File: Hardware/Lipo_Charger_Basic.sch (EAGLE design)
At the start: 14 parts, among them U1 MCP73831, X1 Micro USB

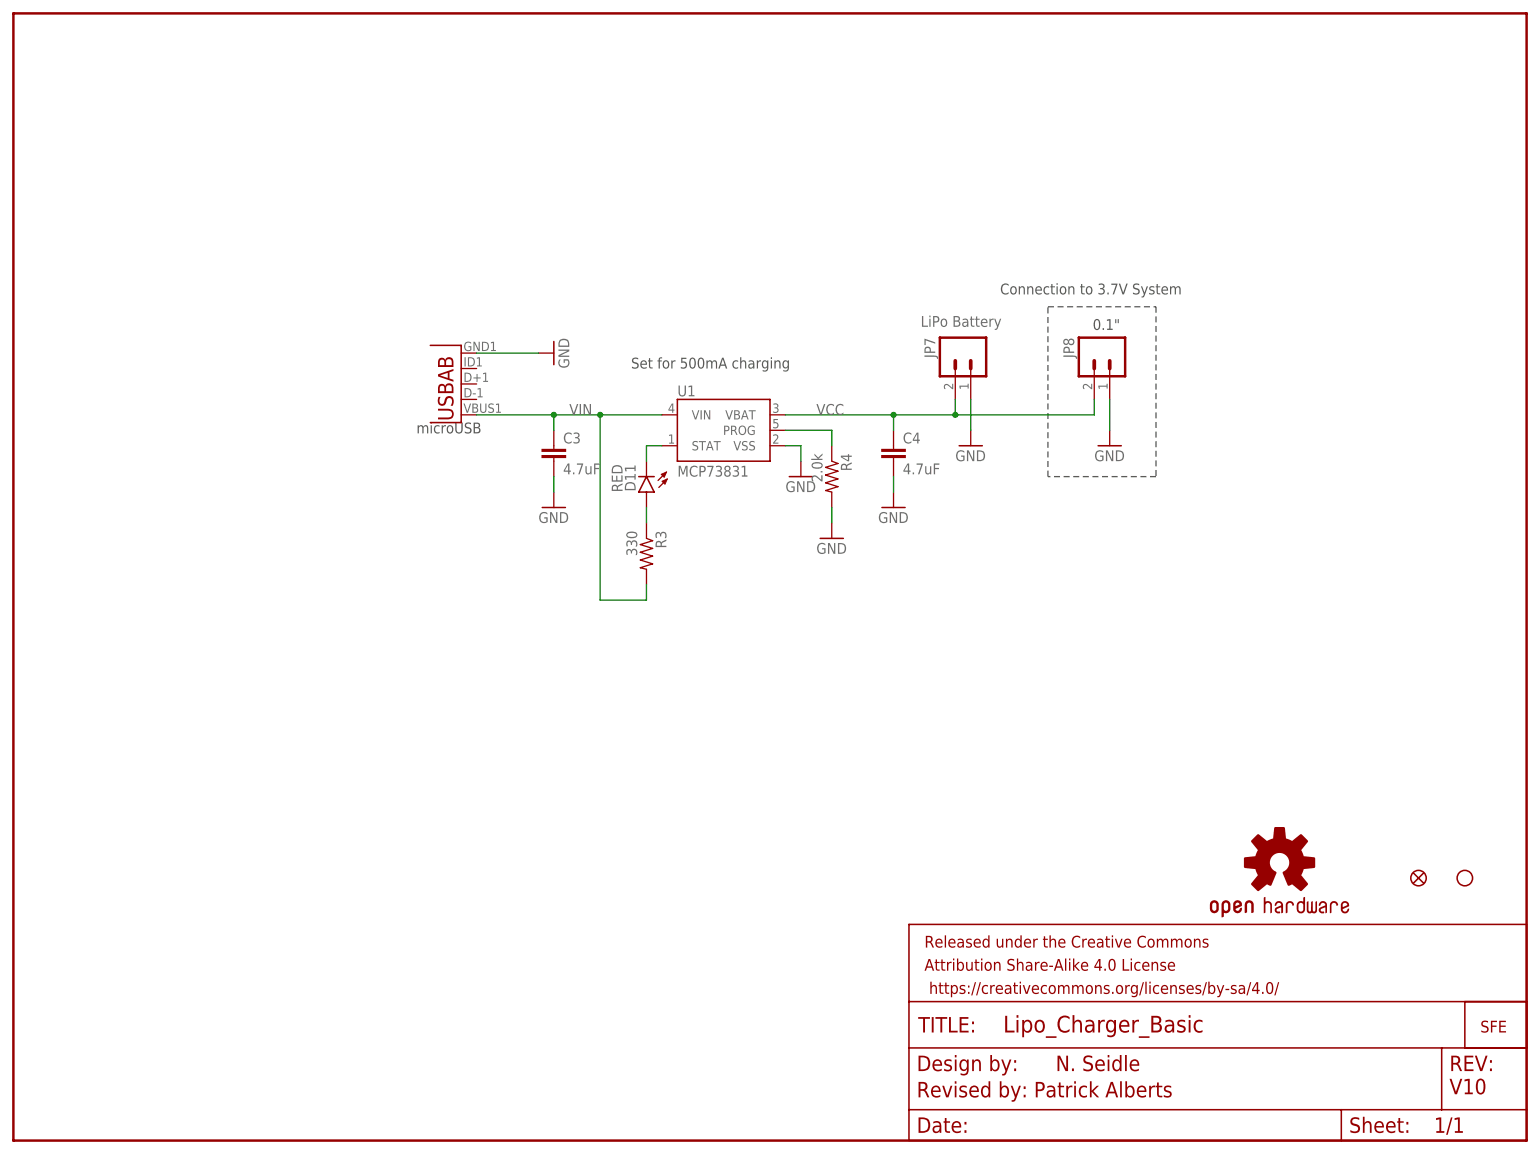
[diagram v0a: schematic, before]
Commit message: Fixed sch and moved micro B
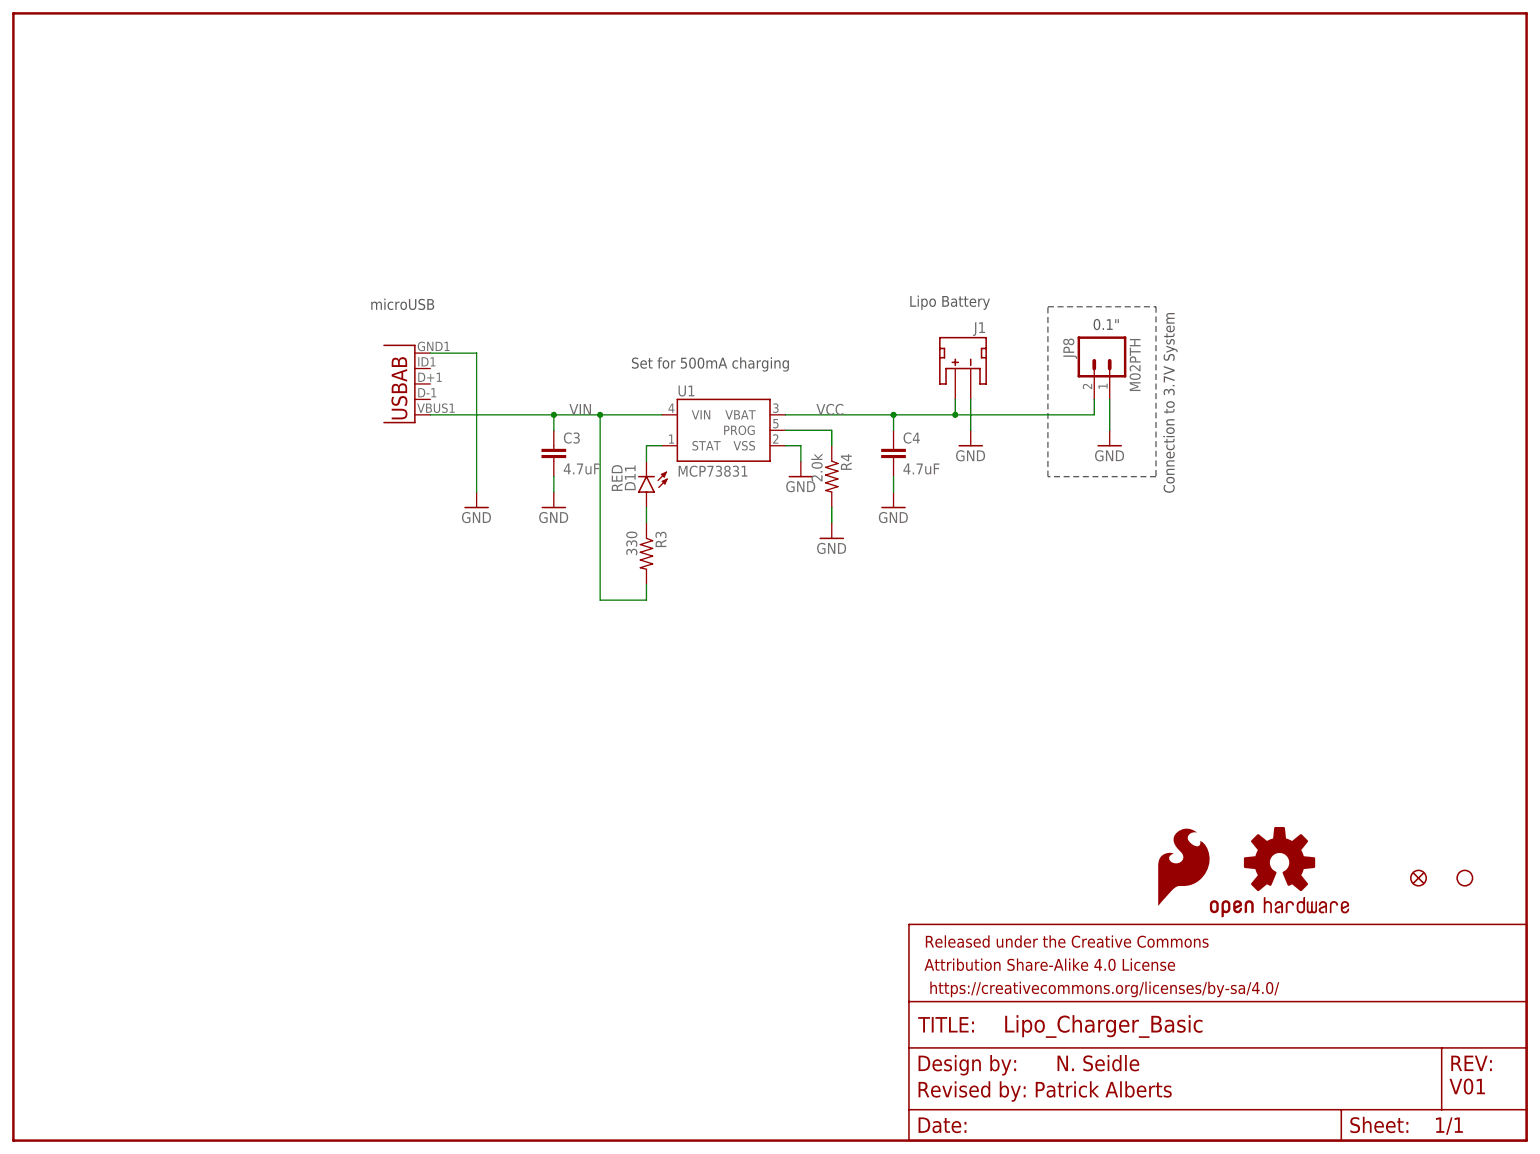
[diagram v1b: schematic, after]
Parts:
- removed JP1: LOGO-SFESK, SparkFun:LOGO-SFESK
- removed JP7: LiPo Battery, SparkFun:M02-JST-2MM-SMT
- removed X1: Micro USB, SparkFun-Connectors:USB-ABCONN-11794
- added GND: Micro USB, SparkFun-Connectors:USB-ABCONN-11794
- added J1: (no value), SparkFun-Connectors:JST_2MM_MALE
- added LOGO2: SFE_LOGO_FLAME.1_INCH, SparkFun-Aesthetics:SFE_LOGO_FLAME.1_INCH
- JP8: value (none) -> M02PTH; device SparkFun:M02PTH -> SparkFun-Connectors:M02PTH
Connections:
- net GND: now also GND.GND, J1.-; no longer JP7.1, X1.GND
- net VCC: now also J1.+; no longer JP7.2
- net VIN: now also GND.VBUS; no longer X1.VBUS
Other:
- note added: "Lipo Battery"
- note added: "V01"
- note removed: "V10"
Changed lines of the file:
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@@
 <?xml version="1.0" encoding="utf-8"?>
 <!DOCTYPE eagle SYSTEM "eagle.dtd">
-<eagle version="7.1.0">
+<eagle version="6.4">
 <drawing>
 <settings>
@@
 <layer number="56" name="wert" color="7" fill="1" visible="no" active="no"/>
 <layer number="57" name="tCAD" color="7" fill="1" visible="no" active="no"/>
+<layer number="90" name="Modules" color="5" fill="1" visible="yes" active="yes"/>
 <layer number="91" name="Nets" color="2" fill="1" visible="yes" active="yes"/>
 <layer number="92" name="Busses" color="1" fill="1" visible="yes" active="yes"/>
@@
 <part name="R4" library="SparkFun-Resistors" deviceset="2.0KOHM1/10W5%(0603)" device="" value="2.0k"/>
 <part name="GND19" library="SparkFun" deviceset="GND" device=""/>
-<part name="JP1" library="SparkFun" deviceset="LOGO-SFE" device="SK"/>
 <part name="JP2" library="SparkFun" deviceset="STAND-OFF" device=""/>
 <part name="C3" library="SparkFun-Capacitors" deviceset="4.7UF-6.3V-10%(0603)" device="0603" value="4.7uF"/>
 <part name="C4" library="SparkFun-Capacitors" deviceset="4.7UF-6.3V-10%(0603)" device="0603" value="4.7uF"/>
-<part name="JP7" library="SparkFun" deviceset="M02" device="-JST-2MM-SMT" value="LiPo Battery"/>
-<part name="JP8" library="SparkFun" deviceset="M02" device="PTH"/>
+<part name="JP8" library="SparkFun-Connectors" deviceset="M02" device="PTH"/>
 <part name="GND2" library="SparkFun" deviceset="GND" device=""/>
-<part name="X1" library="SparkFun-Connectors" deviceset="USB-AB" device="CONN-11794" value="Micro USB"/>
+<part name="GND" library="SparkFun-Connectors" deviceset="USB-AB" device="CONN-11794" value="Micro USB"/>
 <part name="JP3" library="SparkFun" deviceset="FIDUCIAL" device="1X2"/>
 <part name="LOGO1" library="SparkFun-Aesthetics" deviceset="OSHW-LOGO" device="S"/>
+<part name="LOGO2" library="SparkFun-Aesthetics" deviceset="SFE_LOGO_FLAME" device=".1_INCH"/>
+<part name="J1" library="SparkFun-Connectors" deviceset="JST_2MM_MALE" device=""/>
 </parts>
 <sheets>
@@
 <wire x1="170.18" y1="109.22" x2="170.18" y2="137.16" width="0.2032" layer="97" style="longdash"/>
 <text x="101.6" y="127" size="1.778" layer="97">Set for 500mA charging</text>
-<text x="162.306" y="139.192" size="1.778" layer="97">Connection to 3.7V System</text>
+<text x="191.008" y="106.426" size="1.778" layer="97" rot="R90">Connection to 3.7V System</text>
 <text x="177.546" y="133.35" size="1.778" layer="97">0.1"</text>
 <text x="171.45" y="11.43" size="2.54" layer="94">N. Seidle</text>
-<text x="66.294" y="116.332" size="1.778" layer="97">microUSB</text>
+<text x="58.674" y="136.652" size="1.778" layer="97">microUSB</text>
 <text x="148.59" y="7.112" size="2.54" layer="94">Revised by: Patrick Alberts</text>
-<text x="236.22" y="7.62" size="2.54" layer="94">V10</text>
+<text x="236.22" y="7.62" size="2.54" layer="94">V01</text>
+<text x="147.32" y="137.16" size="1.778" layer="97">Lipo Battery</text>
 </plain>
 <instances>
@@
 <instance part="D11" gate="G$1" x="104.14" y="106.68" rot="R180"/>
 <instance part="R3" gate="G$1" x="104.14" y="96.52" rot="R270"/>
-<instance part="GND15" gate="1" x="88.9" y="129.54" rot="R90"/>
+<instance part="GND15" gate="1" x="76.2" y="104.14"/>
 <instance part="GND14" gate="1" x="144.78" y="104.14"/>
 <instance part="GND17" gate="1" x="88.9" y="104.14"/>
@@
 <instance part="R4" gate="G$1" x="134.62" y="109.22" rot="R270"/>
 <instance part="GND19" gate="1" x="134.62" y="99.06"/>
-<instance part="JP1" gate="G$1" x="241.3" y="17.78"/>
 <instance part="JP2" gate="G$1" x="238.76" y="43.18"/>
 <instance part="C3" gate="G$1" x="88.9" y="111.76"/>
 <instance part="C4" gate="G$1" x="144.78" y="111.76"/>
-<instance part="JP7" gate="G$1" x="157.48" y="129.54" smashed="yes" rot="MR270">
-<attribute name="NAME" x="151.638" y="132.08" size="1.778" layer="95" rot="MR270"/>
-<attribute name="VALUE" x="162.56" y="133.858" size="1.778" layer="96" rot="MR0"/>
-</instance>
 <instance part="JP8" gate="G$1" x="180.34" y="129.54" rot="MR270"/>
 <instance part="GND2" gate="1" x="180.34" y="114.3"/>
-<instance part="X1" gate="G$1" x="71.12" y="124.46" rot="MR0"/>
+<instance part="GND" gate="G$1" x="63.5" y="124.46" rot="MR0"/>
 <instance part="JP3" gate="G$1" x="231.14" y="43.18"/>
 <instance part="LOGO1" gate="G$1" x="208.28" y="45.72"/>
+<instance part="LOGO2" gate="G$1" x="187.96" y="38.1"/>
+<instance part="J1" gate="G$1" x="157.48" y="127" rot="MR0"/>
 </instances>
 <busses>
@@
 </segment>
 <segment>
-<wire x1="76.2" y1="129.54" x2="86.36" y2="129.54" width="0.1524" layer="91"/>
+<wire x1="68.58" y1="129.54" x2="76.2" y2="129.54" width="0.1524" layer="91"/>
+<wire x1="76.2" y1="129.54" x2="76.2" y2="106.68" width="0.1524" layer="91"/>
 <pinref part="GND15" gate="1" pin="GND"/>
-<pinref part="X1" gate="G$1" pin="GND"/>
+<pinref part="GND" gate="G$1" pin="GND"/>
 </segment>
 <segment>
@@
 <segment>
 <wire x1="157.48" y1="121.92" x2="157.48" y2="116.84" width="0.1524" layer="91"/>
-<pinref part="JP7" gate="G$1" pin="1"/>
 <pinref part="GND1" gate="1" pin="GND"/>
+<pinref part="J1" gate="G$1" pin="-"/>
 </segment>
 </net>
@@
 <pinref part="C4" gate="G$1" pin="1"/>
 <pinref part="JP8" gate="G$1" pin="2"/>
-<pinref part="JP7" gate="G$1" pin="2"/>
+<pinref part="J1" gate="G$1" pin="+"/>
 </segment>
 </net>
@@
 <wire x1="104.14" y1="88.9" x2="96.52" y2="88.9" width="0.1524" layer="91"/>
 <wire x1="96.52" y1="88.9" x2="96.52" y2="119.38" width="0.1524" layer="91"/>
-<wire x1="76.2" y1="119.38" x2="88.9" y2="119.38" width="0.1524" layer="91"/>
+<wire x1="68.58" y1="119.38" x2="88.9" y2="119.38" width="0.1524" layer="91"/>
 <junction x="88.9" y="119.38"/>
 <junction x="96.52" y="119.38"/>
@@
 <pinref part="U1" gate="G$1" pin="VIN"/>
 <pinref part="C3" gate="G$1" pin="1"/>
-<pinref part="X1" gate="G$1" pin="VBUS"/>
-</segment>
-</net>
+<pinref part="GND" gate="G$1" pin="VBUS"/>
+</segment>
+</net>

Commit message: Computer Change update.
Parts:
- added JP4: FIDUCIAL1X2, SparkFun:FIDUCIAL1X2
- added R1: (no value), SparkFun-Resistors:RESISTORPTH-1/4W-VERT-KIT
- renumbered GND to JP9, J1 to JP1
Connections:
- net GND: now also R1.1
- net PROG: now also R1.2
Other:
- note added: "V10"
- note removed: "V01"
- moved on the sheet: R4
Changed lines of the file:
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@@
 <part name="JP8" library="SparkFun-Connectors" deviceset="M02" device="PTH"/>
 <part name="GND2" library="SparkFun" deviceset="GND" device=""/>
-<part name="GND" library="SparkFun-Connectors" deviceset="USB-AB" device="CONN-11794" value="Micro USB"/>
+<part name="JP9" library="SparkFun-Connectors" deviceset="USB-AB" device="CONN-11794" value="Micro USB"/>
 <part name="JP3" library="SparkFun" deviceset="FIDUCIAL" device="1X2"/>
 <part name="LOGO1" library="SparkFun-Aesthetics" deviceset="OSHW-LOGO" device="S"/>
 <part name="LOGO2" library="SparkFun-Aesthetics" deviceset="SFE_LOGO_FLAME" device=".1_INCH"/>
-<part name="J1" library="SparkFun-Connectors" deviceset="JST_2MM_MALE" device=""/>
+<part name="JP1" library="SparkFun-Connectors" deviceset="JST_2MM_MALE" device=""/>
+<part name="JP4" library="SparkFun" deviceset="FIDUCIAL" device="1X2"/>
+<part name="R1" library="SparkFun-Resistors" deviceset="RESISTOR" device="PTH-1/4W-VERT-KIT"/>
 </parts>
 <sheets>
@@
 <text x="58.674" y="136.652" size="1.778" layer="97">microUSB</text>
 <text x="148.59" y="7.112" size="2.54" layer="94">Revised by: Patrick Alberts</text>
-<text x="236.22" y="7.62" size="2.54" layer="94">V01</text>
+<text x="236.22" y="7.62" size="2.54" layer="94">V10</text>
 <text x="147.32" y="137.16" size="1.778" layer="97">Lipo Battery</text>
 </plain>
@@
 <instance part="GND18" gate="1" x="129.54" y="109.22"/>
 <instance part="U1" gate="G$1" x="116.84" y="116.84"/>
-<instance part="R4" gate="G$1" x="134.62" y="109.22" rot="R270"/>
-<instance part="GND19" gate="1" x="134.62" y="99.06"/>
+<instance part="R4" gate="G$1" x="134.62" y="99.06" rot="R270"/>
+<instance part="GND19" gate="1" x="134.62" y="86.36"/>
 <instance part="JP2" gate="G$1" x="238.76" y="43.18"/>
 <instance part="C3" gate="G$1" x="88.9" y="111.76"/>
@@
 <instance part="JP8" gate="G$1" x="180.34" y="129.54" rot="MR270"/>
 <instance part="GND2" gate="1" x="180.34" y="114.3"/>
-<instance part="GND" gate="G$1" x="63.5" y="124.46" rot="MR0"/>
+<instance part="JP9" gate="G$1" x="63.5" y="124.46" rot="MR0"/>
 <instance part="JP3" gate="G$1" x="231.14" y="43.18"/>
 <instance part="LOGO1" gate="G$1" x="208.28" y="45.72"/>
 <instance part="LOGO2" gate="G$1" x="187.96" y="38.1"/>
-<instance part="J1" gate="G$1" x="157.48" y="127" rot="MR0"/>
+<instance part="JP1" gate="G$1" x="157.48" y="127" rot="MR0"/>
+<instance part="JP4" gate="G$1" x="226.06" y="43.18"/>
+<instance part="R1" gate="G$1" x="139.7" y="99.06" rot="R90"/>
 </instances>
 <busses>
@@
 </segment>
 <segment>
-<wire x1="134.62" y1="101.6" x2="134.62" y2="104.14" width="0.1524" layer="91"/>
+<wire x1="134.62" y1="88.9" x2="134.62" y2="91.44" width="0.1524" layer="91"/>
 <pinref part="R4" gate="G$1" pin="2"/>
 <pinref part="GND19" gate="1" pin="GND"/>
+<pinref part="R1" gate="G$1" pin="1"/>
+<wire x1="134.62" y1="91.44" x2="134.62" y2="93.98" width="0.1524" layer="91"/>
+<wire x1="139.7" y1="93.98" x2="139.7" y2="91.44" width="0.1524" layer="91"/>
+<wire x1="139.7" y1="91.44" x2="134.62" y2="91.44" width="0.1524" layer="91"/>
+<junction x="134.62" y="91.44"/>
 </segment>
 <segment>
@@
 <wire x1="76.2" y1="129.54" x2="76.2" y2="106.68" width="0.1524" layer="91"/>
 <pinref part="GND15" gate="1" pin="GND"/>
-<pinref part="GND" gate="G$1" pin="GND"/>
+<pinref part="JP9" gate="G$1" pin="GND"/>
 </segment>
 <segment>
@@
 <wire x1="157.48" y1="121.92" x2="157.48" y2="116.84" width="0.1524" layer="91"/>
 <pinref part="GND1" gate="1" pin="GND"/>
-<pinref part="J1" gate="G$1" pin="-"/>
+<pinref part="JP1" gate="G$1" pin="-"/>
 </segment>
 </net>
@@
 <pinref part="C4" gate="G$1" pin="1"/>
 <pinref part="JP8" gate="G$1" pin="2"/>
-<pinref part="J1" gate="G$1" pin="+"/>
+<pinref part="JP1" gate="G$1" pin="+"/>
 </segment>
 </net>
@@
 <segment>
 <wire x1="127" y1="116.84" x2="134.62" y2="116.84" width="0.1524" layer="91"/>
-<wire x1="134.62" y1="116.84" x2="134.62" y2="114.3" width="0.1524" layer="91"/>
+<wire x1="134.62" y1="116.84" x2="134.62" y2="106.68" width="0.1524" layer="91"/>
 <pinref part="U1" gate="G$1" pin="PROG"/>
 <pinref part="R4" gate="G$1" pin="1"/>
+<pinref part="R1" gate="G$1" pin="2"/>
+<wire x1="134.62" y1="106.68" x2="134.62" y2="104.14" width="0.1524" layer="91"/>
+<wire x1="139.7" y1="104.14" x2="139.7" y2="106.68" width="0.1524" layer="91"/>
+<wire x1="139.7" y1="106.68" x2="134.62" y2="106.68" width="0.1524" layer="91"/>
+<junction x="134.62" y="106.68"/>
 </segment>
 </net>
@@
 <pinref part="U1" gate="G$1" pin="VIN"/>
 <pinref part="C3" gate="G$1" pin="1"/>
-<pinref part="GND" gate="G$1" pin="VBUS"/>
+<pinref part="JP9" gate="G$1" pin="VBUS"/>
 </segment>
 </net>

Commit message: qc checklist issues fixed.
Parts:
- JP1: value (none) -> JST
- U1: device SparkFun:MCP73831 -> SparkFun-PowerIC:MCP73831
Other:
- note added: "V01"
- note removed: "V10"
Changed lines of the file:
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@@
 <layer number="251" name="SMDround" color="12" fill="11" visible="no" active="no"/>
 <layer number="254" name="cooling" color="7" fill="1" visible="yes" active="yes"/>
+<layer number="255" name="routoute" color="7" fill="1" visible="yes" active="yes"/>
 </layers>
 <schematic xreflabel="%F%N/%S.%C%R" xrefpart="/%S.%C%R">
@@
 <part name="GND17" library="SparkFun" deviceset="GND" device=""/>
 <part name="GND18" library="SparkFun" deviceset="GND" device=""/>
-<part name="U1" library="SparkFun" deviceset="MCP73831" device=""/>
+<part name="U1" library="SparkFun-PowerIC" deviceset="MCP73831" device=""/>
 <part name="R4" library="SparkFun-Resistors" deviceset="2.0KOHM1/10W5%(0603)" device="" value="2.0k"/>
 <part name="GND19" library="SparkFun" deviceset="GND" device=""/>
@@
 <part name="LOGO1" library="SparkFun-Aesthetics" deviceset="OSHW-LOGO" device="S"/>
 <part name="LOGO2" library="SparkFun-Aesthetics" deviceset="SFE_LOGO_FLAME" device=".1_INCH"/>
-<part name="JP1" library="SparkFun-Connectors" deviceset="JST_2MM_MALE" device=""/>
+<part name="JP1" library="SparkFun-Connectors" deviceset="JST_2MM_MALE" device="" value="JST"/>
 <part name="JP4" library="SparkFun" deviceset="FIDUCIAL" device="1X2"/>
 <part name="R1" library="SparkFun-Resistors" deviceset="RESISTOR" device="PTH-1/4W-VERT-KIT"/>
@@
 <text x="177.546" y="133.35" size="1.778" layer="97">0.1"</text>
 <text x="171.45" y="11.43" size="2.54" layer="94">N. Seidle</text>
-<text x="58.674" y="136.652" size="1.778" layer="97">microUSB</text>
+<text x="58.674" y="123.952" size="1.778" layer="97">microUSB</text>
 <text x="148.59" y="7.112" size="2.54" layer="94">Revised by: Patrick Alberts</text>
-<text x="236.22" y="7.62" size="2.54" layer="94">V10</text>
+<text x="236.22" y="7.62" size="2.54" layer="94">V01</text>
 <text x="147.32" y="137.16" size="1.778" layer="97">Lipo Battery</text>
 </plain>
@@
 <instance part="D11" gate="G$1" x="104.14" y="106.68" rot="R180"/>
 <instance part="R3" gate="G$1" x="104.14" y="96.52" rot="R270"/>
-<instance part="GND15" gate="1" x="76.2" y="104.14"/>
+<instance part="GND15" gate="1" x="73.66" y="101.6"/>
 <instance part="GND14" gate="1" x="144.78" y="104.14"/>
 <instance part="GND17" gate="1" x="88.9" y="104.14"/>
@@
 <instance part="JP8" gate="G$1" x="180.34" y="129.54" rot="MR270"/>
 <instance part="GND2" gate="1" x="180.34" y="114.3"/>
-<instance part="JP9" gate="G$1" x="63.5" y="124.46" rot="MR0"/>
+<instance part="JP9" gate="G$1" x="66.04" y="114.3" rot="R180"/>
 <instance part="JP3" gate="G$1" x="231.14" y="43.18"/>
 <instance part="LOGO1" gate="G$1" x="208.28" y="45.72"/>
@@
 </segment>
 <segment>
-<wire x1="68.58" y1="129.54" x2="76.2" y2="129.54" width="0.1524" layer="91"/>
-<wire x1="76.2" y1="129.54" x2="76.2" y2="106.68" width="0.1524" layer="91"/>
 <pinref part="GND15" gate="1" pin="GND"/>
 <pinref part="JP9" gate="G$1" pin="GND"/>
+<wire x1="73.66" y1="104.14" x2="73.66" y2="109.22" width="0.1524" layer="91"/>
+<wire x1="73.66" y1="109.22" x2="71.12" y2="109.22" width="0.1524" layer="91"/>
 </segment>
 <segment>
@@
 <wire x1="104.14" y1="88.9" x2="96.52" y2="88.9" width="0.1524" layer="91"/>
 <wire x1="96.52" y1="88.9" x2="96.52" y2="119.38" width="0.1524" layer="91"/>
-<wire x1="68.58" y1="119.38" x2="88.9" y2="119.38" width="0.1524" layer="91"/>
+<wire x1="71.12" y1="119.38" x2="88.9" y2="119.38" width="0.1524" layer="91"/>
 <junction x="88.9" y="119.38"/>
 <junction x="96.52" y="119.38"/>
